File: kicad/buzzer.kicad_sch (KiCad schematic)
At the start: 7 parts, among them Q1 MMST3904-7-F

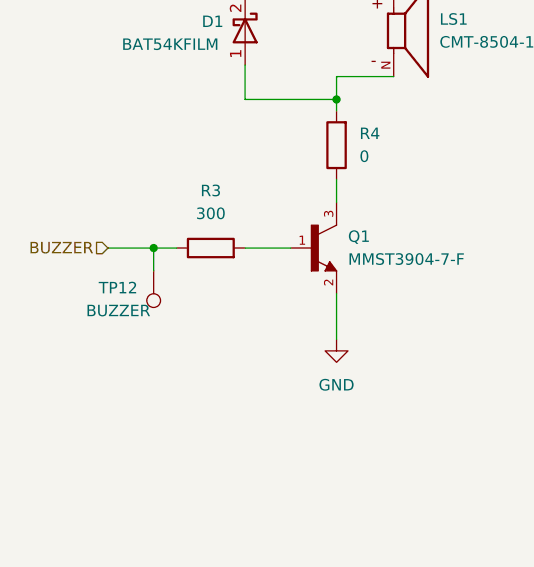
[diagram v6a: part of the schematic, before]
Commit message: feat(PCB): set component-placement example on PCB
This pr will fail due to DRC, skip this and lets have a conversation
about the placement only

Signed-off-by: Bobo Bäck Engström <bobo@id8-engineering.io>
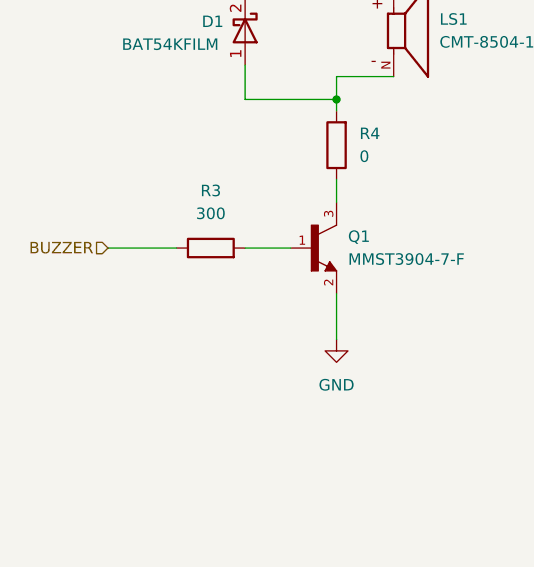
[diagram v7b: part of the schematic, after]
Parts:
- removed TP12: BUZZER, seven-lib:TestPoint_Pad_2.0x2.0mm, symbol seven_lib:TestPoint
- D1: MPN (none) -> BAT54KFILM
- LS1: LCSC (none) -> C22359707; MPN (none) -> CMT-8504-100-SMT-TR
- R3: MPN (none) -> RC0402FR-07300RL
- R4, R5: MPN (none) -> RC0402FR-070RL

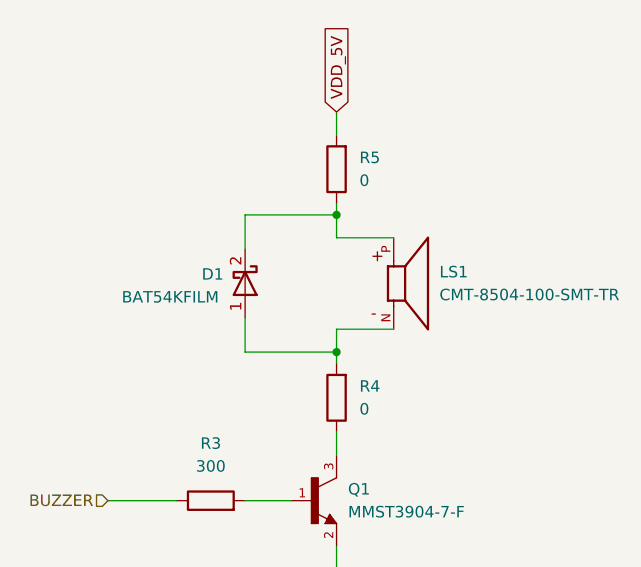
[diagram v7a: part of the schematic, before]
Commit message: fix: fix issues from seven prototype 1
see https://github.com/id8-engineering/seven-bringup/issues/22

Signed-off-by: Bobo Bäck Engström <bobo@id8-engineering.io>
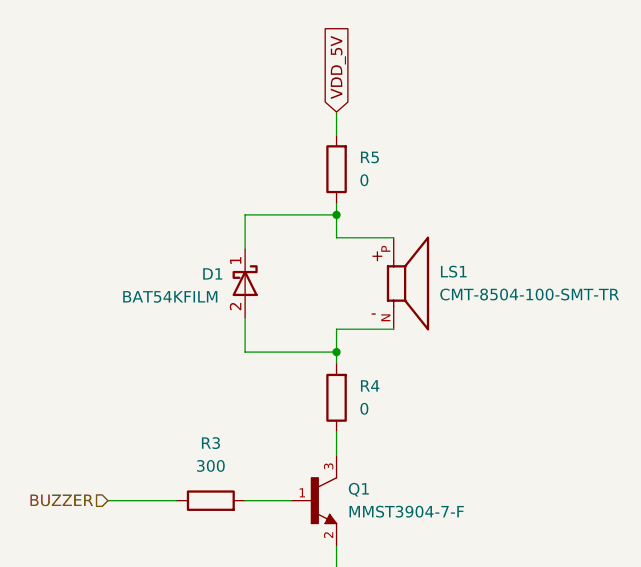
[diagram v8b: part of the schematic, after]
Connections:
- net at LS1.P, R5.1: now also D1.1 (A); no longer D1.2 (K)
- net at LS1.N, R4.2: now also D1.2 (K); no longer D1.1 (A)
